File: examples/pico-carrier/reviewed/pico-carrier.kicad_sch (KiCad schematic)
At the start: 9 parts, among them J1 5V IN, J3 GP0-GP15, J4 GP16-GP28, PWR, U1 Pico

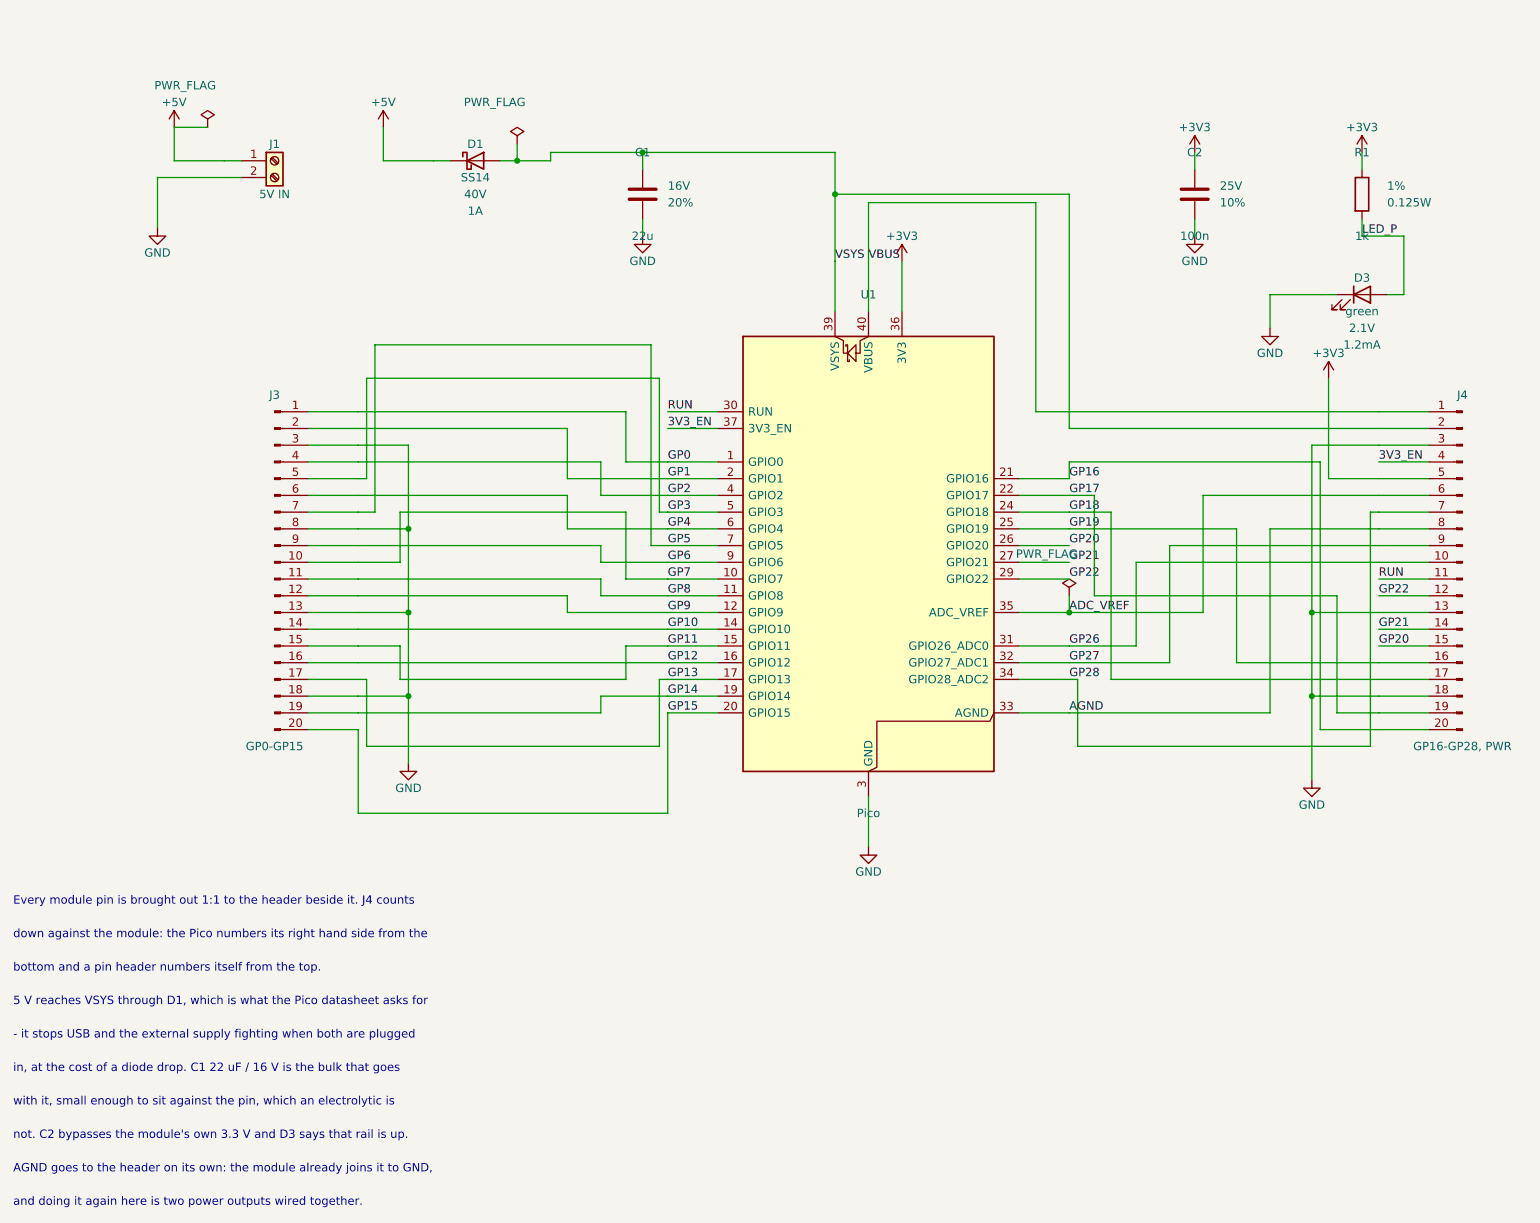
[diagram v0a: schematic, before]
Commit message: Regenerate the five as round three drew them
All five reviewed projects pass their gates again: the buck all wire
with its feedback drawn home, the motor's logic named at the header,
the carrier reading as the pinout table it is - with its feed diode
finally pointing the right way - the filter compact with test points,
and the FPGA's capacitors sitting beside the units they feed. Thirty
renders redrawn, verdict tables at today's numbers.

Co-Authored-By: Claude Fable 5 <noreply@anthropic.com>
Claude-Session: https://claude.ai/code/session_01DUj7Ltu92tWg159mCSacwY
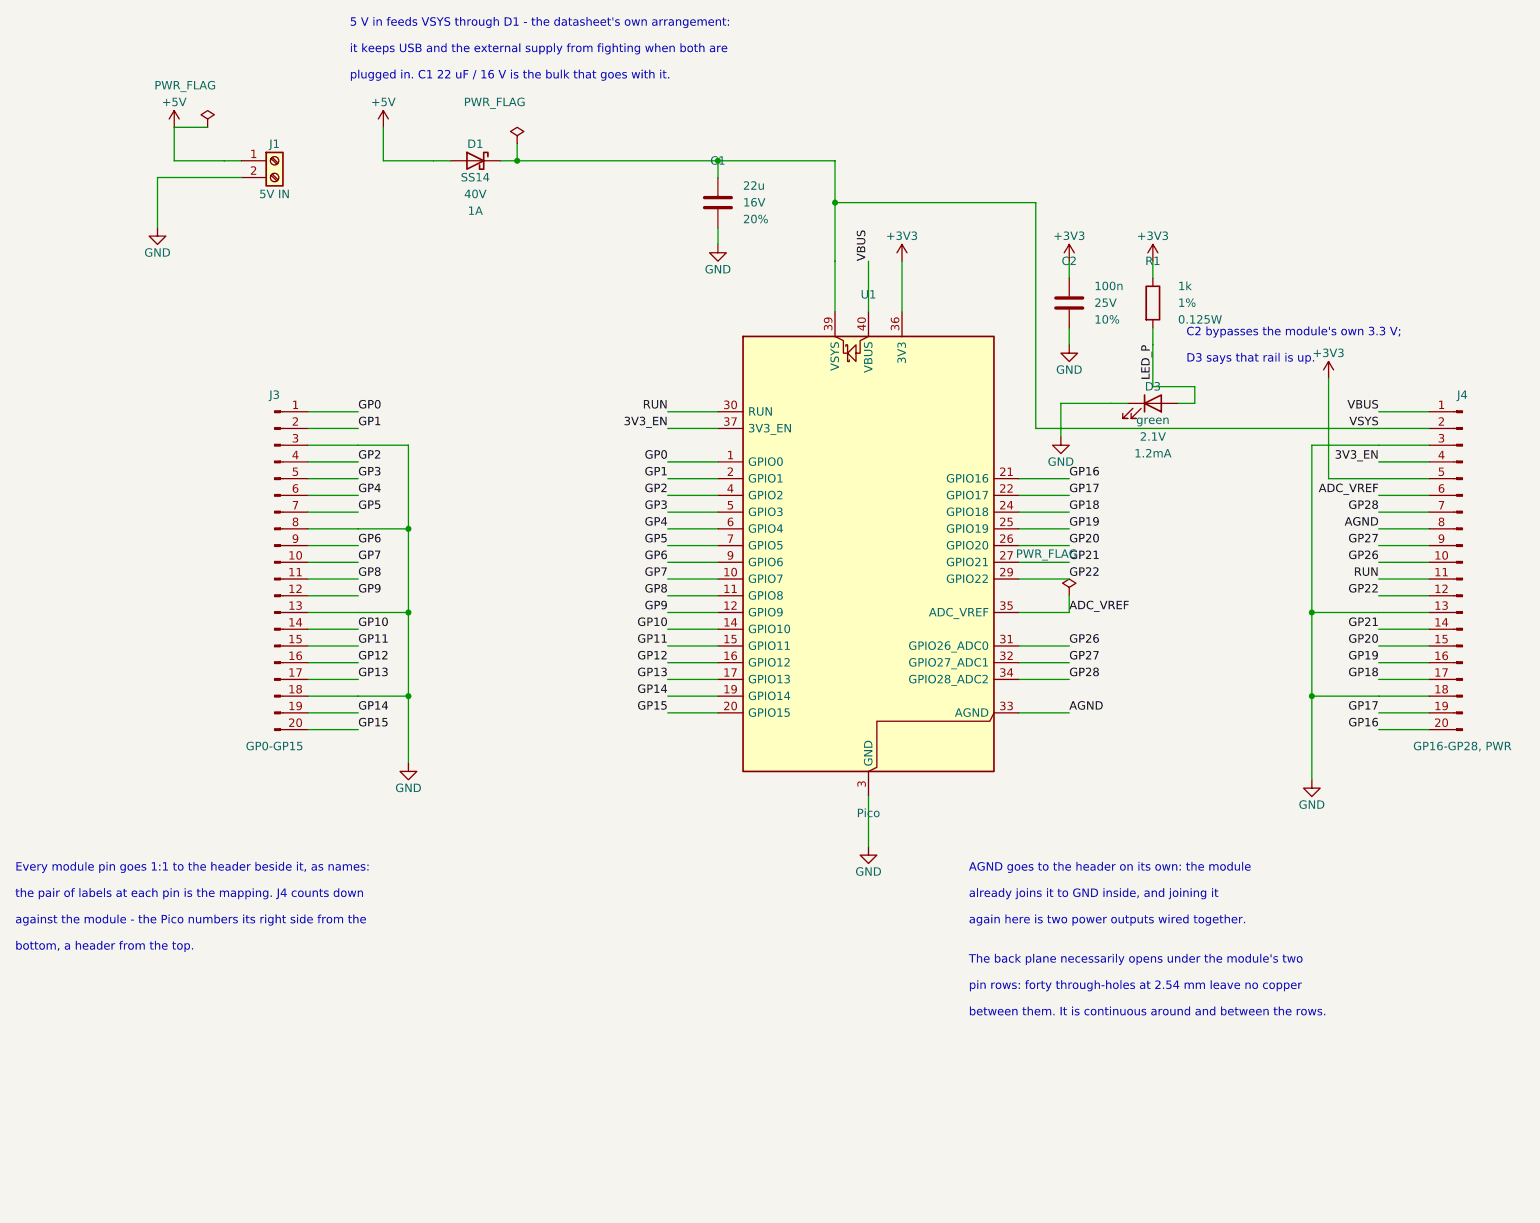
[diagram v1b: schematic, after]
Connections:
- net +5V: now also D1.2 (A); no longer D1.1 (K)
- net VSYS: now also D1.1 (K); no longer D1.2 (A)
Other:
- note added: "5 V in feeds VSYS through D1 - the datasheet's own arrangement:"
- note added: "AGND goes to the header on its own: the module"
- note added: "C2 bypasses the module's own 3.3 V;"
- note added: "D3 says that rail is up."
- note added: "Every module pin goes 1:1 to the header beside it, as names:"
- note added: "The back plane necessarily opens under the module's two"
- note added: "again here is two power outputs wired together."
- note added: "against the module - the Pico numbers its right side from the"
- note added: "already joins it to GND inside, and joining it"
- note added: "between them. It is continuous around and between the rows."
- note added: "bottom, a header from the top."
- note added: "it keeps USB and the external supply from fighting when both are"
- note added: "pin rows: forty through-holes at 2.54 mm leave no copper"
- note added: "plugged in. C1 22 uF / 16 V is the bulk that goes with it."
- note added: "the pair of labels at each pin is the mapping. J4 counts down"
- note removed: "- it stops USB and the external supply fighting when both are plugged"
- note removed: "5 V reaches VSYS through D1, which is what the Pico datasheet asks for"
- note removed: "AGND goes to the header on its own: the module already joins it to GND,"
- note removed: "Every module pin is brought out 1:1 to the header beside it. J4 counts"
- note removed: "and doing it again here is two power outputs wired together."
- note removed: "bottom and a pin header numbers itself from the top."
- note removed: "down against the module: the Pico numbers its right hand side from the"
- note removed: "in, at the cost of a diode drop. C1 22 uF / 16 V is the bulk that goes"
- note removed: "not. C2 bypasses the module's own 3.3 V and D3 says that rail is up."
- note removed: "with it, small enough to sit against the pin, which an electrolytic is"
- moved on the sheet: C1, C2, D3, R1

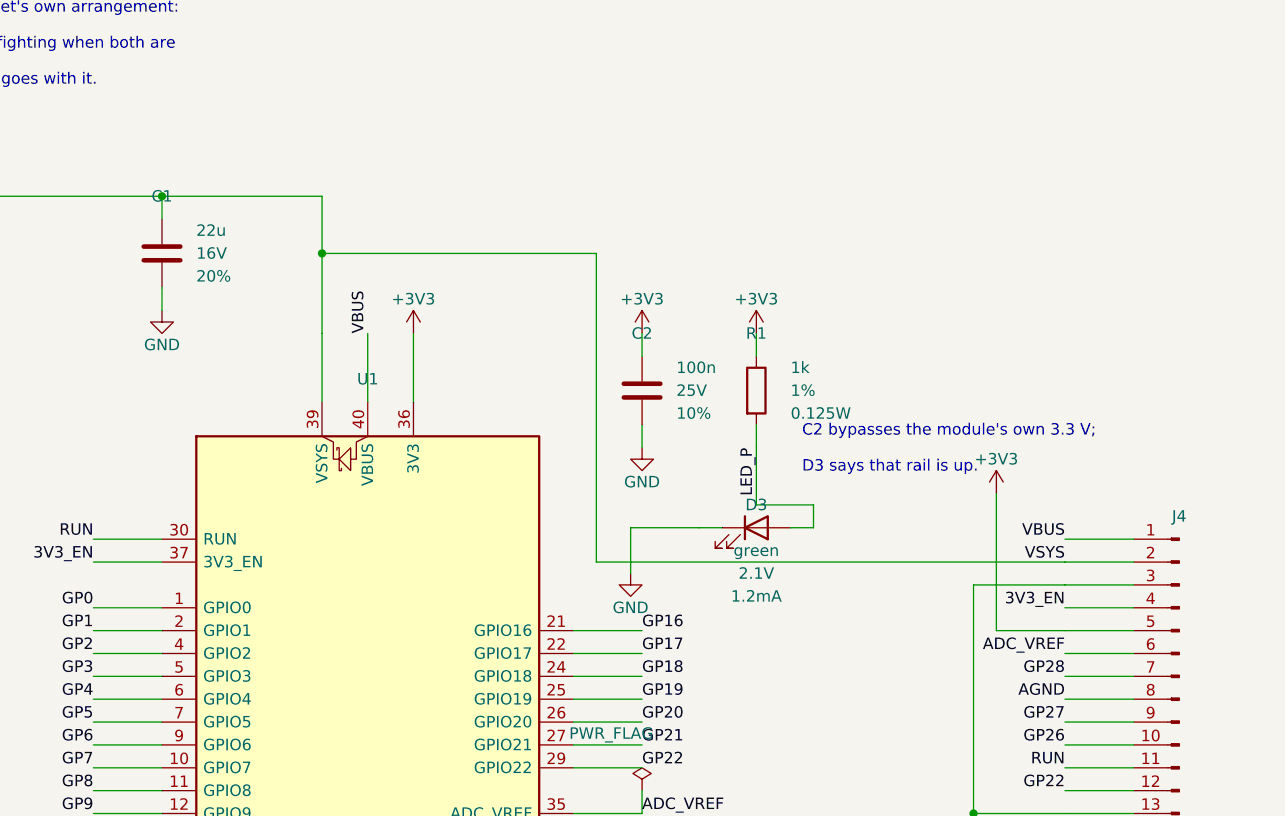
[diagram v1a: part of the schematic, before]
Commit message: Regenerate the four boards round four has settled
The buck, the motor driver, the carrier and the filter as the current
generator draws them: interior ground stitching on all four, the motor
driver's bundle tight and its board twelve millimetres shorter, the
filter compact and hand-placed, the carrier's indicator in a column of
its own. All four pass their gates. The FPGA is still regenerating.

Co-Authored-By: Claude Fable 5 <noreply@anthropic.com>
Claude-Session: https://claude.ai/code/session_01DUj7Ltu92tWg159mCSacwY
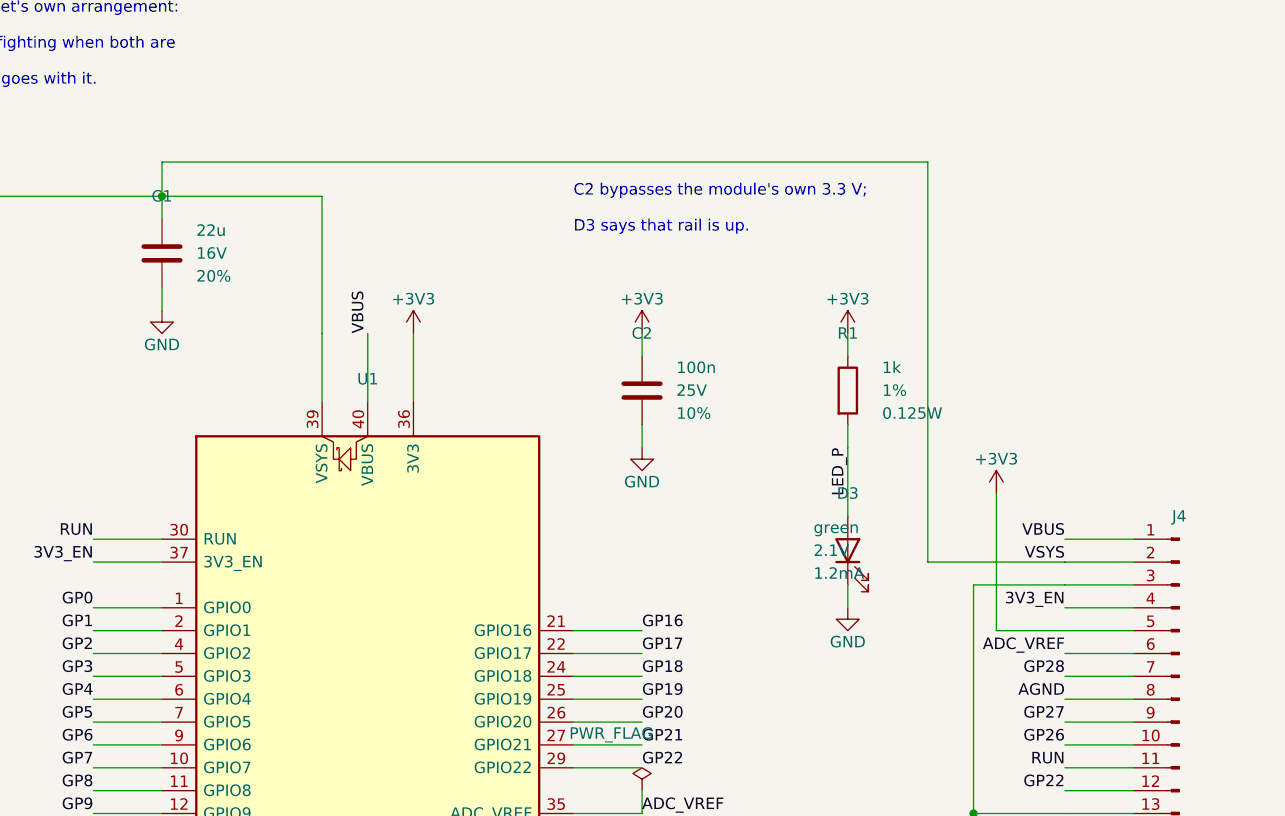
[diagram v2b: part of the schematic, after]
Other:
- moved on the sheet: D3, R1
